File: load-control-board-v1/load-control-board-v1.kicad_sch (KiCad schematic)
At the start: 7 parts, among them Q1 BSC026N08NS5, U1 LM741

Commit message: opamp part
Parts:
- added C2: C, symbol Device:C
- added R5: 1k, symbol Device:R
- added R6: 9k, symbol Device:R
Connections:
- net +5V: now also C2.1
- net GND: now also C2.2, R6.1
- net VDC: no longer names the net of U1.3 (+)
- net VDC: now also R5.1, R6.2
- new net I_CTRL: R5.2

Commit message: communicate 1
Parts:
- removed R2, R3, R4: R, symbol Device:R
- removed U1: LM741, symbol Amplifier_Operational:LM741
- added C3, C4: C, symbol Device:C
- added Q2: BSC026N08NS5, Package_TO_SOT_SMD:TDSON-8-1, symbol Transistor_FET:BSC026N08NS5
- added R10: 1m, symbol Device:R
- added R7, R8, R9: R, symbol Device:R
- added RV1, RV2: R_Potentiometer_Trim, symbol Device:R_Potentiometer_Trim
- added U1: 74AHC1G04, symbol 74xGxx:74AHC1G04
- added U2: LM741, symbol Amplifier_Operational:LM741
- added U3: LM7805_TO220, Package_TO_SOT_THT:TO-220-3_Vertical, symbol Regulator_Linear:LM7805_TO220
- added U4, U5: LM397, Package_TO_SOT_SMD:SOT-23-5, symbol Comparator:LM397
- C1: value C -> 0.22u
- C2: value C -> 0.1u
- R1: value R -> 0
- R5: value 1k -> 100k
- R6: value 9k -> 1k
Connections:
- net GND: now also C1.2, Q1.1 (S), Q1.2 (S), Q1.3 (S), C3.2, R10.1, R8.1, RV1.3, RV2.3, U1.3 (GND), U2.4 (V-), U3.2 (GND), U4.2 (V-), U5.2 (V-)
- net batt+: now also Q2.5 (D), U5.3 (+); no longer Q1.5 (D)
- net at R1.1: now also Q1.5 (D); no longer C1.1
- net at Q1.4 (G): now also U1.4; no longer R1.2
- net V_I_CTRL: now reaches R5.1, R6.2
- net V_I_CTRL: now also R1.2, U2.3 (+)
- net +5V renamed 5V
- net 5V: now also RV1.1, RV2.1, U1.5 (VCC), U3.3 (VO), U4.5 (V+), U5.5 (V+)
- net I_CTRL renamed I_sink
- new net: RV2.2, U5.1 (-)
- new net: C4.1, R7.1, U2.6
- new net: Q2.4 (G), R7.2, R8.2
- new net: C4.2, R9.1, U2.2 (-)
- new net: RV1.2, U4.1 (-)
- new net +12V: C1.1, C3.1, U2.7 (V+), U3.1 (VI)
- new net EN: U1.2
- new net I_mos_mon: Q2.1 (S), Q2.2 (S), Q2.3 (S), R10.2, R9.2, U4.3 (+)
- new net OC_Alert: U4.4
- new net OV_Alert: U5.4
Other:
- note added: "Mos modules, *4"
- moved on the sheet: R5, R6

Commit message: sch half complete
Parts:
- removed U2: LM741, symbol Amplifier_Operational:LM741
- added C5, C9: 100n, symbol Device:C
- added C7, C8: C, symbol Device:C
- added R10, R11, R16, R17: 1k, symbol Device:R
- added R12, R13, R18, R19: 50k, symbol Device:R
- added R14, R15: R, symbol Device:R
- added R2: 1.1k, symbol Device:R
- added R3: 8.2k, symbol Device:R
- added R4: 680, symbol Device:R
- added TP1, TP2, TP3: TestPoint, symbol Connector:TestPoint
- added U2, U7: OPA188xxDBV, Package_TO_SOT_SMD:TSOT-23-5, symbol Amplifier_Operational:OPA188xxDBV
- added U6: PZ127-2-10-S, programmable-load-library:HDR-SMD_PZ127-2-10-S, symbol programmable-load-library:PZ127-2-10-S
- C3: value C -> 100n
- C4: value C -> 50n
- R7: value R -> 100
- R8: value R -> 10k
- R9: value R -> 500
- renumbered R10 to Rs0
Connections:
- net +12V: now also C3.2, C5.2, C9.2, U2.5 (V+), U7.5 (V+); no longer C3.1
- net GND: now also C3.1, C5.1, C7.1, C8.1, C9.1, R11.2, R13.2, R17.2, R18.2, R2.1, U2.2 (V-), U7.2 (V-); no longer C3.2
- net V_I_CTRL: now also TP2.1, U2.3 (+)
- net batt+: now also R3.2; no longer U5.3 (+)
- net at C4.1, R7.1: now also U2.1
- net at C4.2, R9.1: now also U2.4 (-)
- net I_mos_mon renamed V_Rs0p
- net V_Rs0p: now also R10.2, R16.2; no longer R9.2, U4.3 (+)
- new net: C8.2, R15.2, U4.3 (+)
- new net: R10.1, R13.1, U7.3 (+)
- new net: R19.1, TP3.1
- new net: R12.1, R9.2, TP1.1, U7.1
- new net: R11.1, R12.2, U7.4 (-)
- new net: C7.2, R14.2, U5.3 (+)
- new net: R16.1, R18.1
- new net: R17.1, R19.2
- new net: R3.1, R4.2
- new net I_sink_mon_0: R15.1
- new net Vbus_mon: R14.1, R2.2, R4.1
- no-connect marks 2 -> 0
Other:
- moved on the sheet: C1, C2, C3, C4, Q2, R7, R8, R9, RV1, RV2, Rs0, U3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

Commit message: pre-final sch
add channel 0-4
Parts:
- removed C3, C5, C9: 100n, symbol Device:C
- removed C4: 50n, symbol Device:C
- removed Q2: BSC026N08NS5, Package_TO_SOT_SMD:TDSON-8-1, symbol Transistor_FET:BSC026N08NS5
- removed R10, R11, R16, R17, R6: 1k, symbol Device:R
- removed R12, R13, R18, R19: 50k, symbol Device:R
- removed R5: 100k, symbol Device:R
- removed R7: 100, symbol Device:R
- removed R8: 10k, symbol Device:R
- removed R9: 500, symbol Device:R
- removed Rs0: 1m, symbol Device:R
- removed TP1, TP2, TP3: TestPoint, symbol Connector:TestPoint
- removed U2, U7: OPA188xxDBV, Package_TO_SOT_SMD:TSOT-23-5, symbol Amplifier_Operational:OPA188xxDBV
- C1, C2, C7, C8: footprint (none) -> Capacitor_SMD:C_0603_1608Metric
- R1, R14, R15, R2, R3, R4: footprint (none) -> Resistor_SMD:R_0603_1608Metric
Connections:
- net V_I_CTRL is gone; now on net I_sink: R1.2
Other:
- added sheet ch0 (channel.kicad_sch)
- added sheet ch1 (channel.kicad_sch)
- added sheet ch2 (channel.kicad_sch)
- added sheet ch3 (channel.kicad_sch)
- note removed: "Mos modules, *4"
- moved on the sheet: C1, C2, C7, C8, Q1, R1, R14, R15, R2, R3, R4, RV1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

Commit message: lc2kicad
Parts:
- added C37, C38, C39: 100n, Capacitor_SMD:C_0603_1608Metric, symbol Device:C
- C7, C8: value C -> 100n
- R14, R15: value R -> 500
- U1: footprint (none) -> Package_TO_SOT_SMD:SOT-23-5
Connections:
- net 5V: now also C37.2, C38.2, C39.2
- net GND: now also C37.1, C38.1, C39.1
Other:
- sheet ch0 ports: added I_sink_mon; removed none
- sheet ch1 ports: added I_sink_mon; removed none
- sheet ch2 ports: added I_sink_mon; removed none
- sheet ch3 ports: added I_sink_mon; removed none
- moved on the sheet: U6

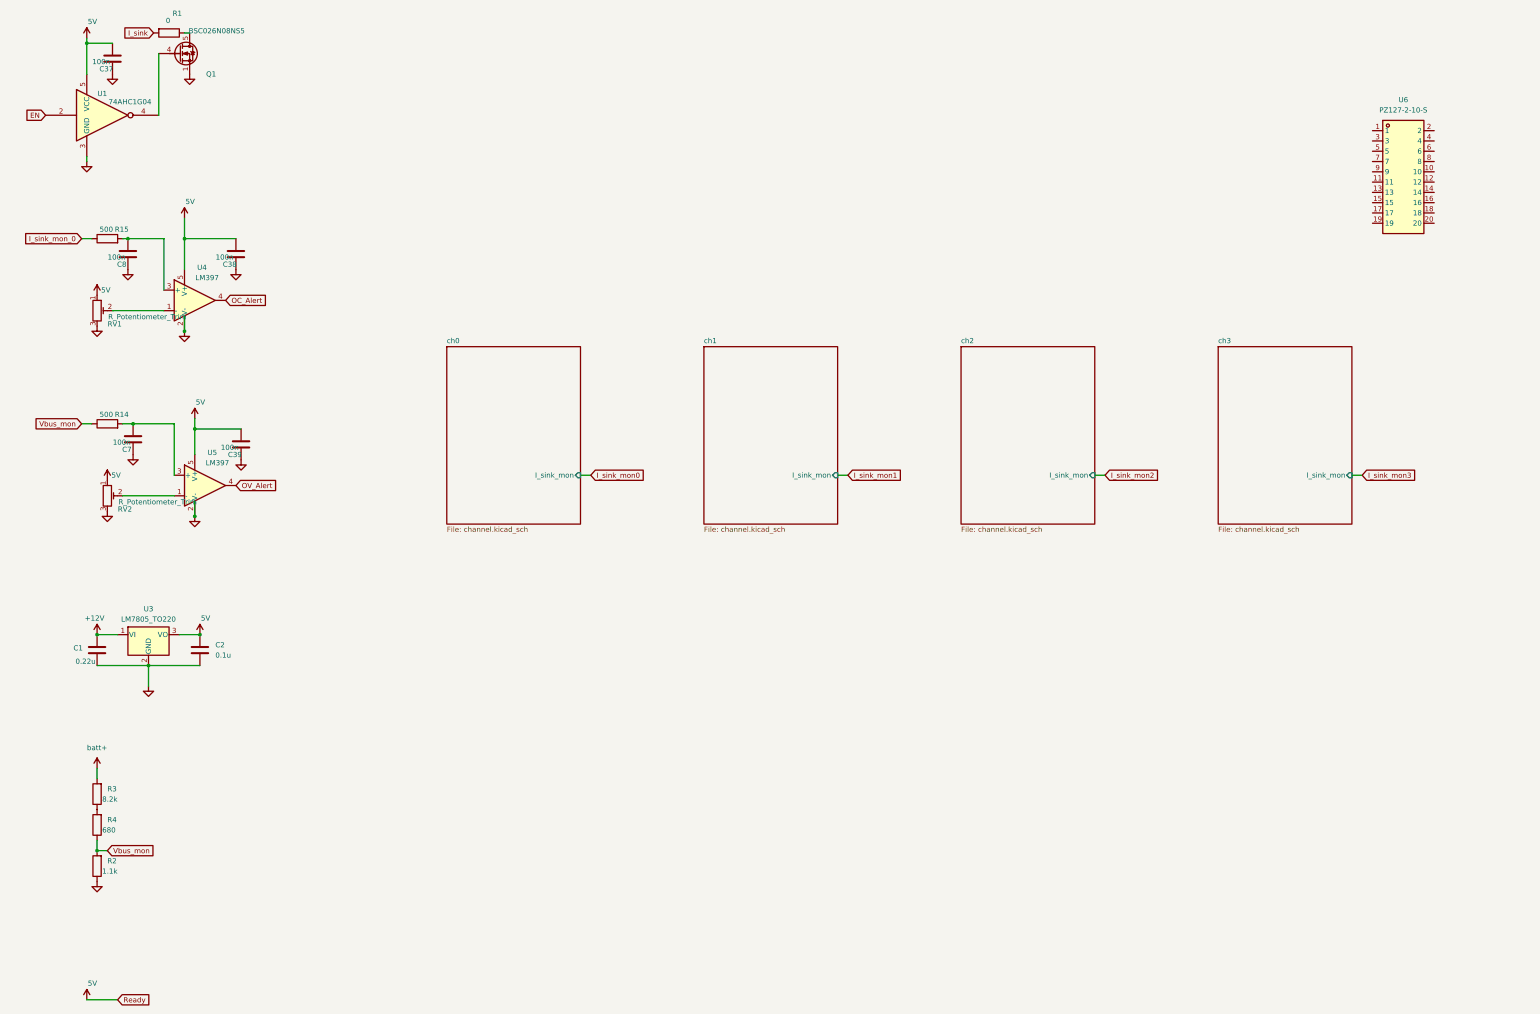
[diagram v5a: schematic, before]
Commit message: Edit multi opamp
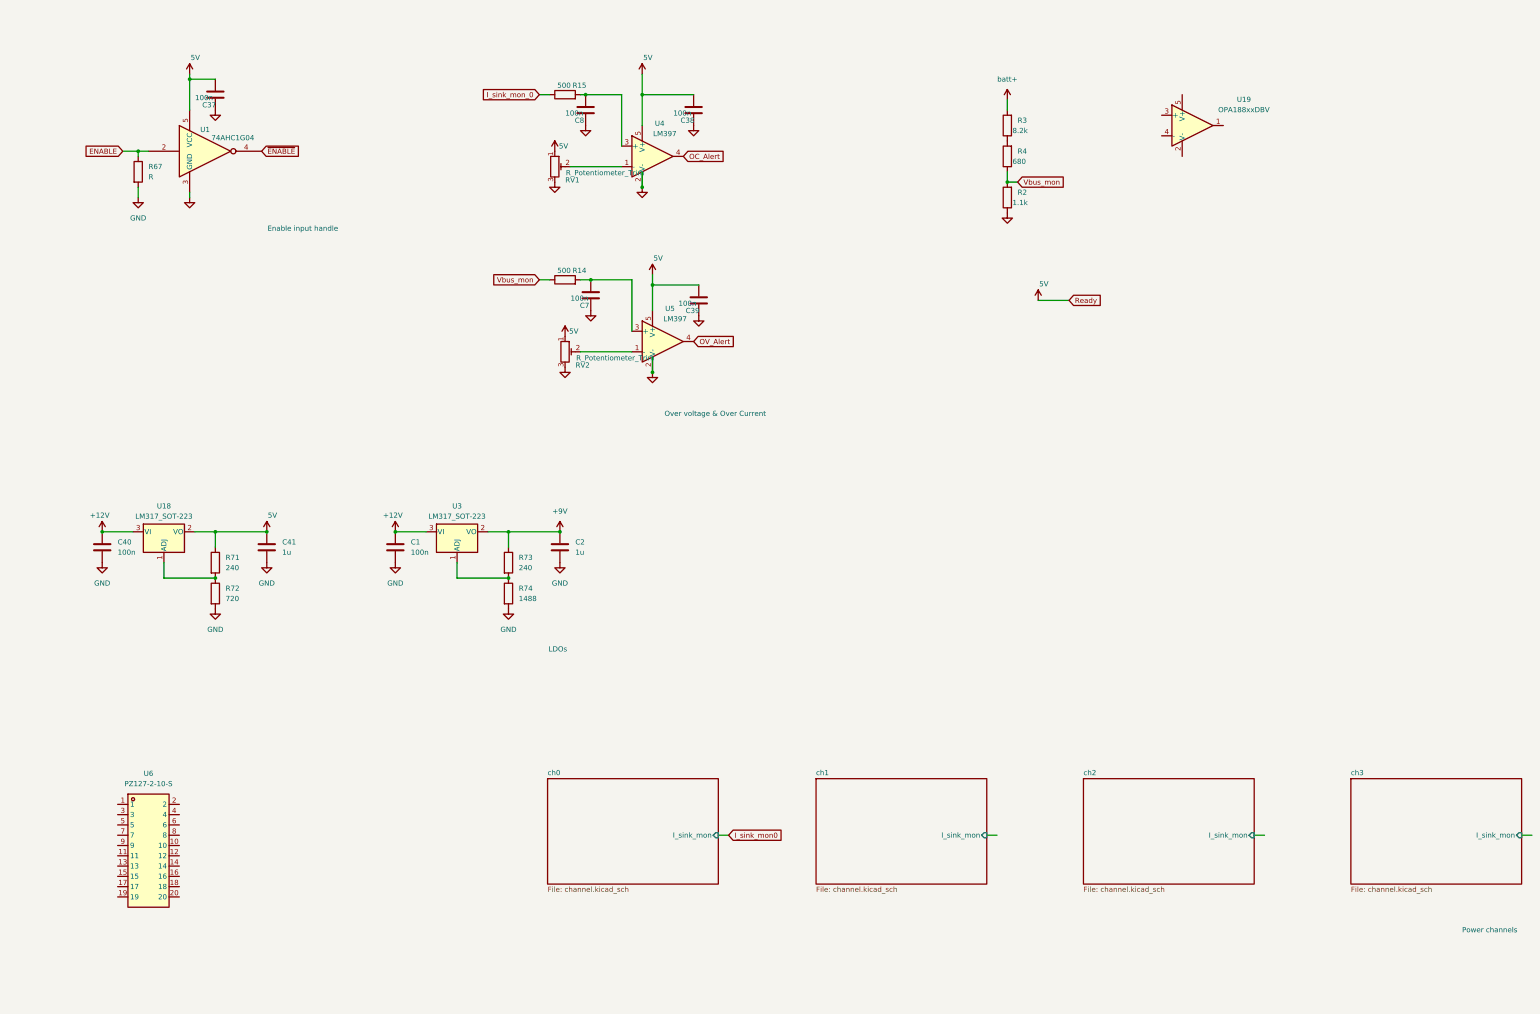
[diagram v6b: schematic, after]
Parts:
- removed Q1: BSC026N08NS5, Package_TO_SOT_SMD:TDSON-8-1, symbol Transistor_FET:BSC026N08NS5
- removed R1: 0, Resistor_SMD:R_0603_1608Metric, symbol Device:R
- removed U3: LM7805_TO220, Package_TO_SOT_THT:TO-220-3_Vertical, symbol Regulator_Linear:LM7805_TO220
- added C40: 100n, symbol Device:C
- added C41: 1u, symbol Device:C
- added R67: R, symbol Device:R
- added R71, R73: 240, symbol Device:R
- added R72: 720, symbol Device:R
- added R74: 1488, symbol Device:R
- added U18, U3: LM317_SOT-223, Package_TO_SOT_SMD:SOT-89-3, symbol Regulator_Linear:LM317_SOT-223
- added U19: OPA188xxDBV, Package_TO_SOT_SMD:TSOT-23-5, symbol Amplifier_Operational:OPA188xxDBV
- C1: value 0.22u -> 100n; footprint Capacitor_SMD:C_0603_1608Metric -> (none)
- C2: value 0.1u -> 1u; footprint Capacitor_SMD:C_0603_1608Metric -> (none)
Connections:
- net +12V: now also C40.1, U18.3 (VI), U3.3 (VI)
- net 5V: now also C41.1, R71.1, U18.2 (VO); no longer C2.1
- net GND: now also C40.2, C41.2, R67.2, R72.2, R74.2
- net ~{ENABLE}: now reaches U1.4
- net EN renamed ENABLE
- net ENABLE: now also R67.1
- new net: R73.2, R74.1, U3.1 (ADJ)
- new net: R71.2, R72.1, U18.1 (ADJ)
- new net +9V: C2.1, R73.1, U3.2 (VO)
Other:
- note added: "Enable input handle"
- note added: "LDOs"
- note added: "Over voltage & Over Current"
- note added: "Power channels"
- moved on the sheet: C37, C38, C39, C7, C8, R14, R15, R2, R3, R4, RV1, RV2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

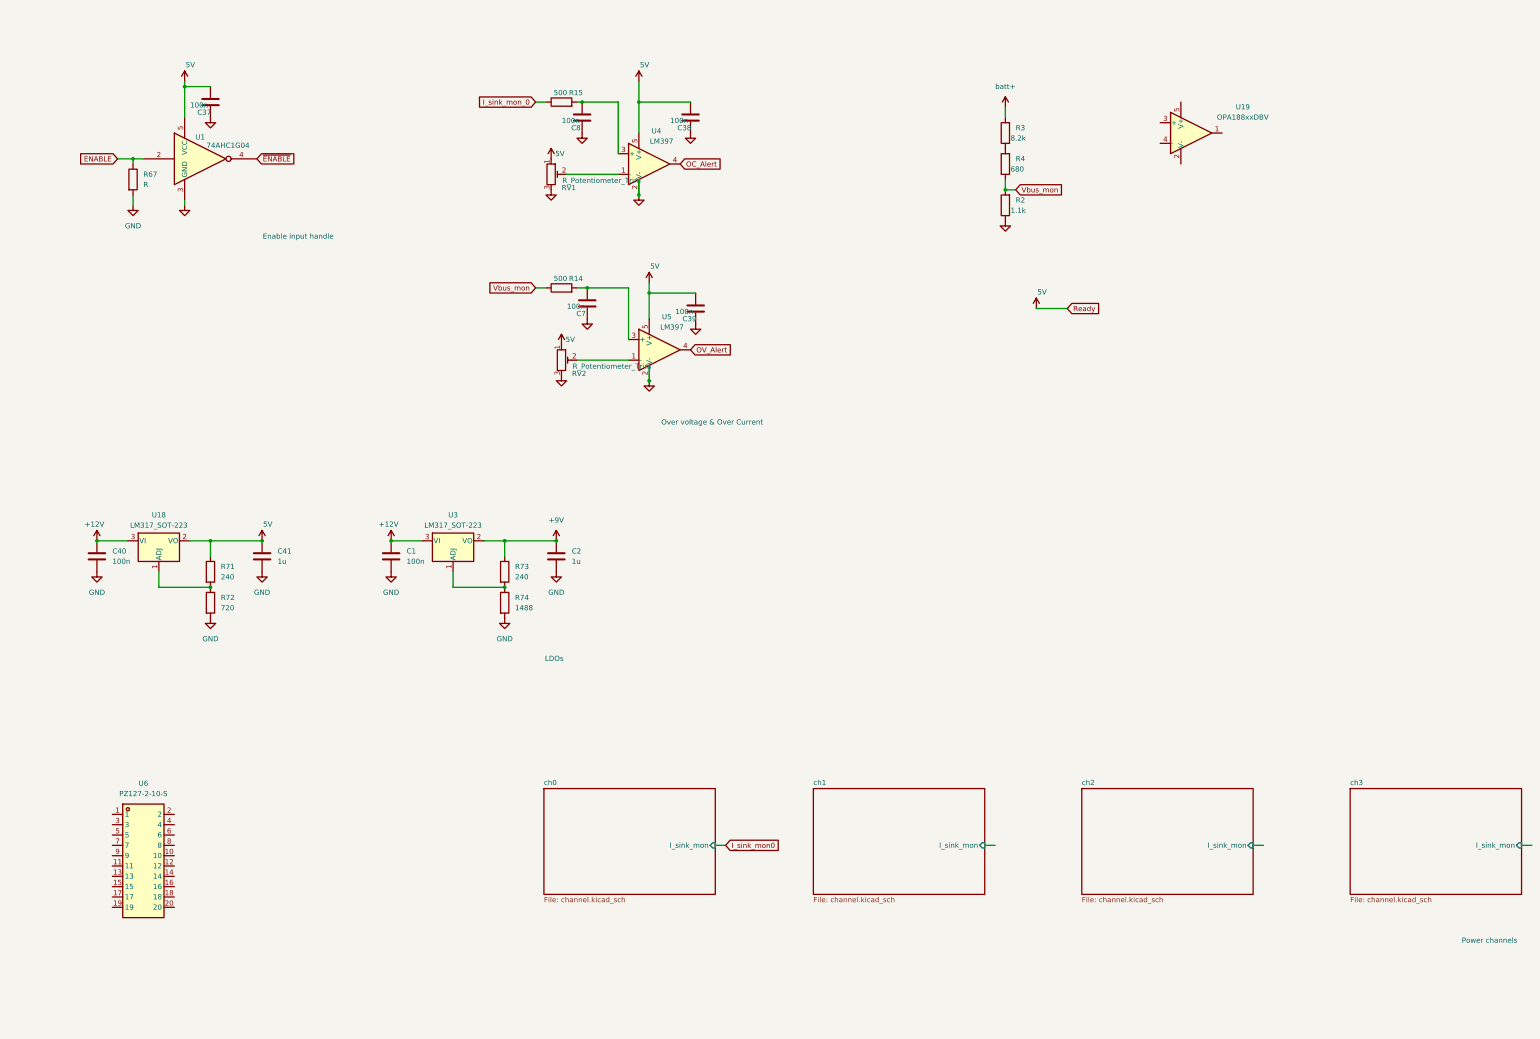
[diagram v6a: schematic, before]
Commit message: Rearrange design in load control board, need further check
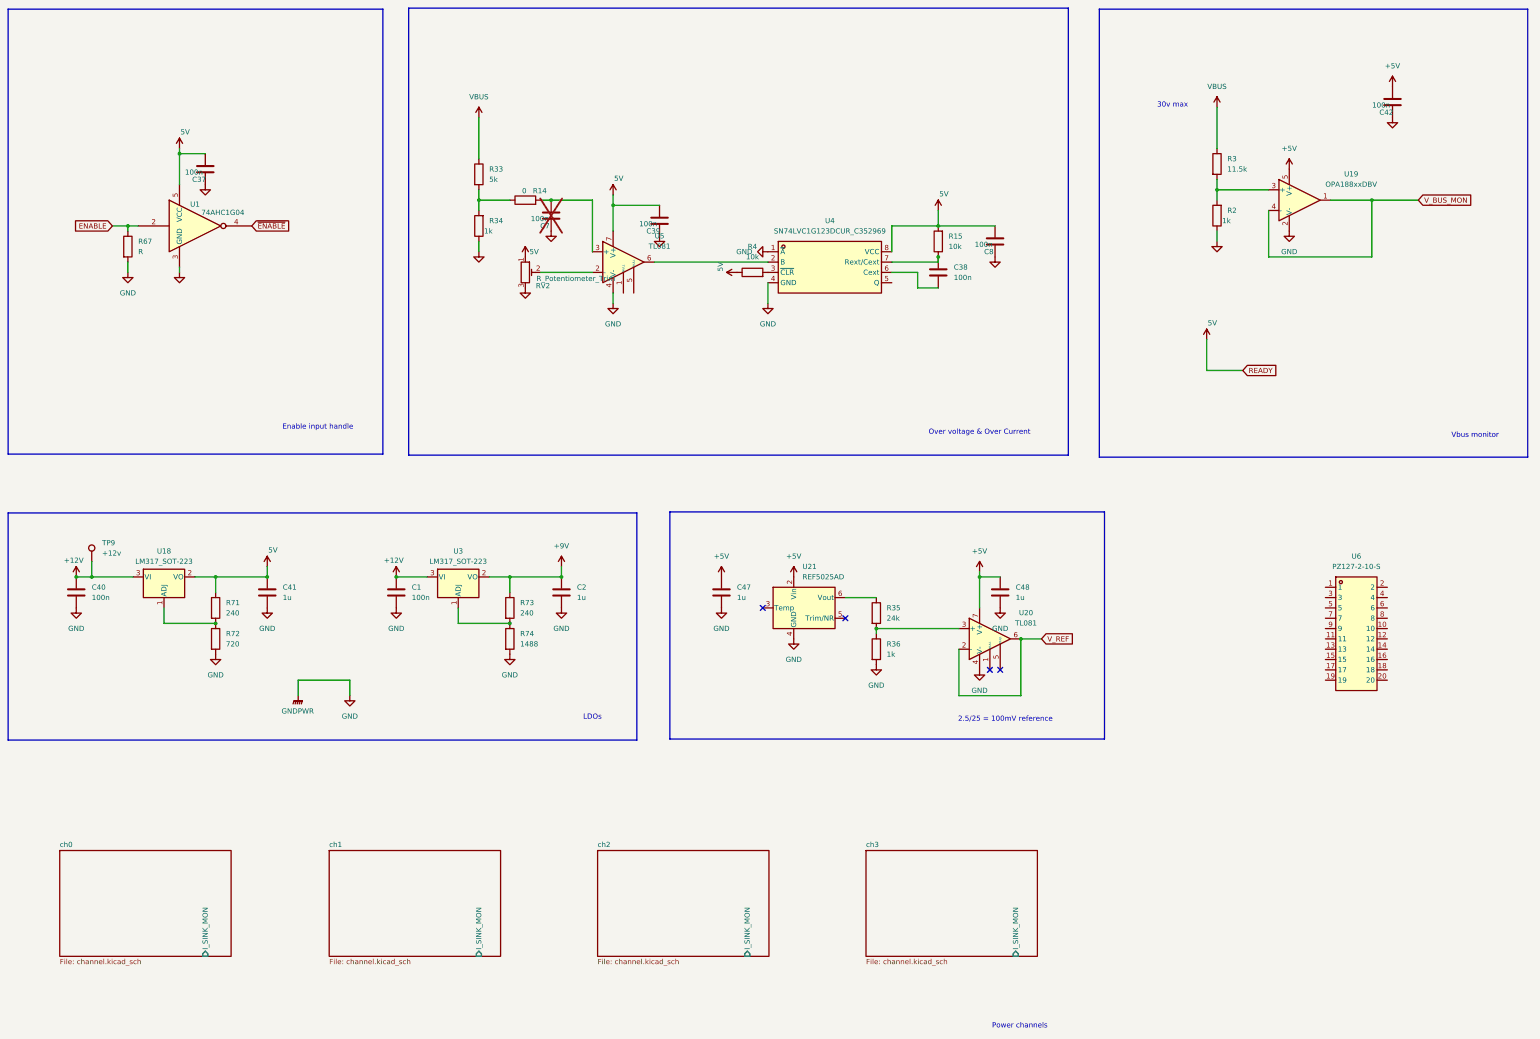
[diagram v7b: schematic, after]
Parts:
- removed RV1: R_Potentiometer_Trim, symbol Device:R_Potentiometer_Trim
- removed U4, U5: LM397, Package_TO_SOT_SMD:SOT-23-5, symbol Comparator:LM397
- added C42: 100n, Capacitor_SMD:C_0603_1608Metric, symbol Device:C
- added C47, C48: 1u, symbol Device:C
- added R33: 5k, symbol Device:R
- added R34: 1k, Resistor_SMD:R_0603_1608Metric, symbol Device:R
- added R35: 24k, symbol Device:R
- added R36: 1k, symbol Device:R
- added TP9: +12v, symbol Connector:TestPoint
- added U20, U5: TL081, symbol Amplifier_Operational:TL081
- added U21: REF5025AD, Package_SO:SOIC-8_3.9x4.9mm_P1.27mm, symbol Reference_Voltage:REF5025AD
- added U4: SN74LVC1G123DCUR_C352969, programmable-load-library:VSSOP-8_L2.3-W2.0-P0.50-LS3.1-BL, symbol programmable-load-library:SN74LVC1G123DCUR_C352969
- C38: footprint Capacitor_SMD:C_0603_1608Metric -> (none)
- C7: now not fitted
- R14: value 500 -> 0
- R15: value 500 -> 10k; footprint Resistor_SMD:R_0603_1608Metric -> (none)
- R2: value 1.1k -> 1k
- R3: value 8.2k -> 11.5k; footprint Resistor_SMD:R_0603_1608Metric -> (none)
- R4: value 680 -> 10k; footprint Resistor_SMD:R_0603_1608Metric -> (none)
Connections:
- net batt+ is gone; now on an unnamed net: R3.2
- net +12V: now also TP9.1
- net 5V: now also C8.2, R15.2, R4.1, U4.8 (VCC), U5.7 (V+); no longer C38.2
- net GND: now also U19.2 (V-), C42.1, C47.2, C48.2, R34.1, R36.2, U20.4 (V-), U21.4 (GND), U4.1 (~{A}), U4.4 (GND), U5.4 (V-); no longer C38.1
- net at RV2.2: now also U5.2 (-)
- net V_BUS_MON: now reaches U19.1
- net V_BUS_MON: now also U19.4 (-)
- net at U19.3 (+): now also R2.2
- net +5V: now reaches U19.5 (V+)
- net +5V: now also C42.2, C47.1, C48.1, U20.7 (V+), U21.2 (Vin)
- net at C7.2, R14.2: now also U5.3 (+)
- net at R4.2: now also U4.3 (~{CLR}); no longer R3.1
- net I_sink_mon_0: no longer names the net of R15.1
- net I_sink_mon_0: now also C38.1, U4.7 (Rext/Cext)
- removed net Vbus_mon: R14.1, R2.2, R4.1
- new net: R35.1, U21.6 (Vout)
- new net: R35.2, R36.1, U20.3 (+)
- new net: R14.1, R33.2, R34.2
- new net: U4.2 (B), U5.6
- new net: C38.2, U4.6 (Cext)
- new net VBUS: R3.1, R33.1
- new net V_REF: U20.2 (-), U20.6
- no-connect marks 0 -> 4
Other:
- sheet ch0 ports: added I_SINK_MON; removed I_sink_mon
- sheet ch1 ports: added I_SINK_MON; removed I_sink_mon
- sheet ch2 ports: added I_SINK_MON; removed I_sink_mon
- sheet ch3 ports: added I_SINK_MON; removed I_sink_mon
- note added: "2.5/25 = 100mV reference"
- note added: "30v max"
- note added: "Vbus monitor"
- moved on the sheet: C1, C2, C37, C39, C40, C41, R14, R2, R67, R71, R72, R73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
